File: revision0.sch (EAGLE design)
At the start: 93 parts, among them IC1 MSP430FR698X(1)80-PIN_PN, IC3 FT232RL

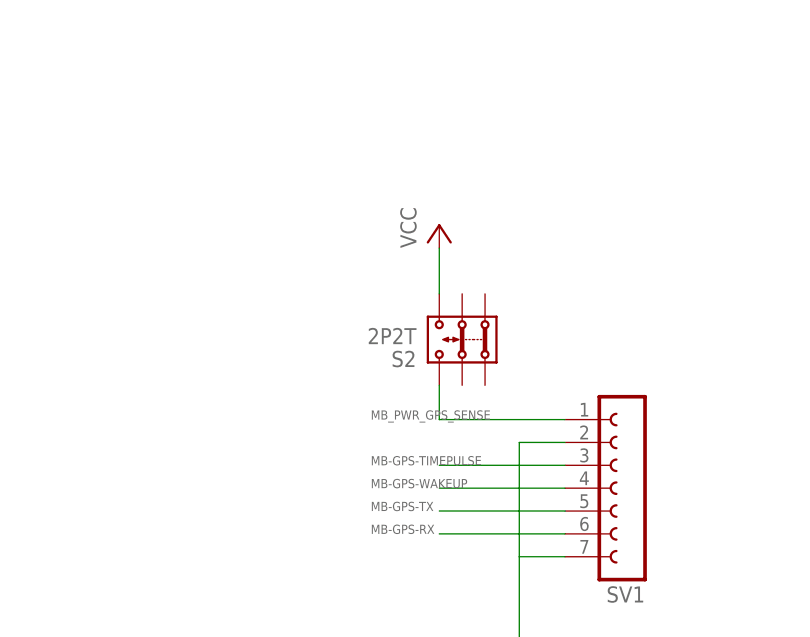
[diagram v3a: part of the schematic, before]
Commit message: Fix CANAL sliding switch
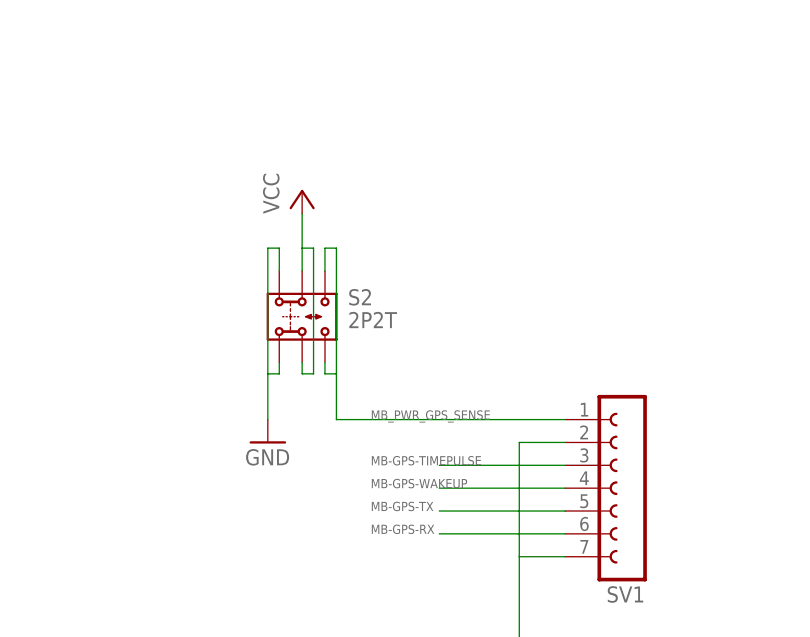
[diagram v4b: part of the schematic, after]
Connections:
- net GND: now also S2.1.1, S2.1.2
- net MB_PWR_GPS_SENSE: now also S2.3.2
- net VCC: now also S2.2.1, S2.2.2; no longer S2.3.2
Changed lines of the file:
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@@
 <grid distance="50" unitdist="mil" unit="mil" style="lines" multiple="1" display="yes" altdistance="0.01" altunitdist="inch" altunit="inch"/>
 <layers>
-<layer number="1" name="Top" color="4" fill="1" visible="no" active="no"/>
-<layer number="16" name="Bottom" color="1" fill="1" visible="no" active="no"/>
-<layer number="17" name="Pads" color="2" fill="1" visible="no" active="no"/>
-<layer number="18" name="Vias" color="2" fill="1" visible="no" active="no"/>
-<layer number="19" name="Unrouted" color="6" fill="1" visible="no" active="no"/>
-<layer number="20" name="Dimension" color="15" fill="1" visible="no" active="no"/>
-<layer number="21" name="tPlace" color="7" fill="1" visible="no" active="no"/>
-<layer number="22" name="bPlace" color="7" fill="1" visible="no" active="no"/>
-<layer number="23" name="tOrigins" color="15" fill="1" visible="no" active="no"/>
-<layer number="24" name="bOrigins" color="15" fill="1" visible="no" active="no"/>
-<layer number="25" name="tNames" color="7" fill="1" visible="no" active="no"/>
-<layer number="26" name="bNames" color="7" fill="1" visible="no" active="no"/>
-<layer number="27" name="tValues" color="7" fill="1" visible="no" active="no"/>
-<layer number="28" name="bValues" color="7" fill="1" visible="no" active="no"/>
+<layer number="1" name="Top" color="4" fill="1" visible="yes" active="no"/>
+<layer number="16" name="Bottom" color="1" fill="1" visible="yes" active="no"/>
+<layer number="17" name="Pads" color="2" fill="1" visible="yes" active="no"/>
+<layer number="18" name="Vias" color="2" fill="1" visible="yes" active="no"/>
+<layer number="19" name="Unrouted" color="6" fill="1" visible="yes" active="no"/>
+<layer number="20" name="Dimension" color="15" fill="1" visible="yes" active="no"/>
+<layer number="21" name="tPlace" color="7" fill="1" visible="yes" active="no"/>
+<layer number="22" name="bPlace" color="7" fill="1" visible="yes" active="no"/>
+<layer number="23" name="tOrigins" color="15" fill="1" visible="yes" active="no"/>
+<layer number="24" name="bOrigins" color="15" fill="1" visible="yes" active="no"/>
+<layer number="25" name="tNames" color="7" fill="1" visible="yes" active="no"/>
+<layer number="26" name="bNames" color="7" fill="1" visible="yes" active="no"/>
+<layer number="27" name="tValues" color="7" fill="1" visible="yes" active="no"/>
+<layer number="28" name="bValues" color="7" fill="1" visible="yes" active="no"/>
 <layer number="29" name="tStop" color="7" fill="3" visible="no" active="no"/>
 <layer number="30" name="bStop" color="7" fill="6" visible="no" active="no"/>
@@
 <layer number="35" name="tGlue" color="7" fill="4" visible="no" active="no"/>
 <layer number="36" name="bGlue" color="7" fill="5" visible="no" active="no"/>
-<layer number="37" name="tTest" color="7" fill="1" visible="no" active="no"/>
-<layer number="38" name="bTest" color="7" fill="1" visible="no" active="no"/>
+<layer number="37" name="tTest" color="7" fill="1" visible="yes" active="no"/>
+<layer number="38" name="bTest" color="7" fill="1" visible="yes" active="no"/>
 <layer number="39" name="tKeepout" color="4" fill="11" visible="no" active="no"/>
 <layer number="40" name="bKeepout" color="1" fill="11" visible="no" active="no"/>
@@
 <layer number="44" name="Drills" color="7" fill="1" visible="no" active="no"/>
 <layer number="45" name="Holes" color="7" fill="1" visible="no" active="no"/>
-<layer number="46" name="Milling" color="3" fill="1" visible="no" active="no"/>
-<layer number="47" name="Measures" color="7" fill="1" visible="no" active="no"/>
-<layer number="48" name="Document" color="7" fill="1" visible="no" active="no"/>
-<layer number="49" name="Reference" color="7" fill="1" visible="no" active="no"/>
-<layer number="51" name="tDocu" color="7" fill="1" visible="no" active="no"/>
-<layer number="52" name="bDocu" color="7" fill="1" visible="no" active="no"/>
+<layer number="46" name="Milling" color="3" fill="1" visible="yes" active="no"/>
+<layer number="47" name="Measures" color="7" fill="1" visible="yes" active="no"/>
+<layer number="48" name="Document" color="7" fill="1" visible="yes" active="no"/>
+<layer number="49" name="Reference" color="7" fill="1" visible="yes" active="no"/>
+<layer number="51" name="tDocu" color="7" fill="1" visible="yes" active="no"/>
+<layer number="52" name="bDocu" color="7" fill="1" visible="yes" active="no"/>
 <layer number="90" name="Modules" color="5" fill="1" visible="yes" active="yes"/>
 <layer number="91" name="Nets" color="2" fill="1" visible="yes" active="yes"/>
@@
 <part name="GND7" library="supply1" deviceset="GND" device=""/>
 <part name="GND12" library="supply1" deviceset="GND" device=""/>
+<part name="GND34" library="supply1" deviceset="GND" device=""/>
 </parts>
 <sheets>
@@
 <instance part="GND6" gate="1" x="-190.5" y="-17.78" rot="R270"/>
 <instance part="P+1" gate="VCC" x="-193.04" y="-35.56" rot="R90"/>
-<instance part="P+3" gate="VCC" x="180.34" y="73.66"/>
+<instance part="P+3" gate="VCC" x="165.1" y="77.47"/>
 <instance part="C3" gate="G$1" x="-175.26" y="-25.4" rot="MR0"/>
 <instance part="C4" gate="G$1" x="-182.88" y="-25.4" rot="MR0"/>
@@
 <instance part="TP-PWRBATT" gate="G$1" x="228.6" y="124.46"/>
 <instance part="GND26" gate="1" x="-119.38" y="-104.14"/>
-<instance part="S2" gate="G$1" x="182.88" y="60.96" rot="R180"/>
+<instance part="S2" gate="G$1" x="165.1" y="63.5"/>
 <instance part="R24" gate="G$1" x="220.98" y="-55.88" rot="R90"/>
 <instance part="R25" gate="G$1" x="213.36" y="-55.88" rot="R90"/>
@@
 <instance part="GND7" gate="1" x="250.19" y="24.13"/>
 <instance part="GND12" gate="1" x="281.94" y="-88.9"/>
+<instance part="GND34" gate="1" x="161.29" y="49.53"/>
 </instances>
 <busses>
@@
 <wire x1="276.86" y1="219.71" x2="276.86" y2="224.79" width="0.1524" layer="91"/>
 <pinref part="JP2" gate="A" pin="2"/>
-</segment>
-<segment>
-<pinref part="P+3" gate="VCC" pin="VCC"/>
-<pinref part="S2" gate="G$1" pin="3.2"/>
-<wire x1="180.34" y1="66.04" x2="180.34" y2="71.12" width="0.1524" layer="91"/>
 </segment>
 <segment>
@@
 <junction x="-449.58" y="38.1"/>
 </segment>
+<segment>
+<pinref part="P+3" gate="VCC" pin="VCC"/>
+<wire x1="165.1" y1="74.93" x2="165.1" y2="71.12" width="0.1524" layer="91"/>
+<pinref part="S2" gate="G$1" pin="2.1"/>
+<wire x1="165.1" y1="71.12" x2="165.1" y2="68.58" width="0.1524" layer="91"/>
+<wire x1="165.1" y1="71.12" x2="166.37" y2="71.12" width="0.1524" layer="91"/>
+<wire x1="166.37" y1="71.12" x2="166.37" y2="57.15" width="0.1524" layer="91"/>
+<pinref part="S2" gate="G$1" pin="2.2"/>
+<wire x1="166.37" y1="57.15" x2="165.1" y2="57.15" width="0.1524" layer="91"/>
+<wire x1="165.1" y1="57.15" x2="165.1" y2="58.42" width="0.1524" layer="91"/>
+</segment>
 </net>
 <net name="GND" class="0">
@@
 <wire x1="250.19" y1="39.37" x2="250.19" y2="26.67" width="0.1524" layer="91"/>
 <wire x1="257.81" y1="39.37" x2="250.19" y2="39.37" width="0.1524" layer="91"/>
+</segment>
+<segment>
+<pinref part="S2" gate="G$1" pin="1.1"/>
+<wire x1="162.56" y1="68.58" x2="162.56" y2="71.12" width="0.1524" layer="91"/>
+<wire x1="162.56" y1="71.12" x2="161.29" y2="71.12" width="0.1524" layer="91"/>
+<wire x1="161.29" y1="71.12" x2="161.29" y2="57.15" width="0.1524" layer="91"/>
+<pinref part="S2" gate="G$1" pin="1.2"/>
+<wire x1="161.29" y1="57.15" x2="162.56" y2="57.15" width="0.1524" layer="91"/>
+<wire x1="162.56" y1="57.15" x2="162.56" y2="58.42" width="0.1524" layer="91"/>
+<pinref part="GND34" gate="1" pin="GND"/>
+<wire x1="161.29" y1="52.07" x2="161.29" y2="57.15" width="0.1524" layer="91"/>
 </segment>
 </net>
@@
 </segment>
 <segment>
-<wire x1="180.34" y1="52.07" x2="194.31" y2="52.07" width="0.1524" layer="91"/>
 <label x="172.72" y="52.07" size="1.016" layer="95"/>
+<pinref part="S2" gate="G$1" pin="3.2"/>
+<wire x1="167.64" y1="58.42" x2="167.64" y2="57.15" width="0.1524" layer="91"/>
 <pinref part="S2" gate="G$1" pin="3.1"/>
-<wire x1="180.34" y1="52.07" x2="180.34" y2="55.88" width="0.1524" layer="91"/>
+<wire x1="167.64" y1="68.58" x2="167.64" y2="71.12" width="0.1524" layer="91"/>
+<wire x1="167.64" y1="71.12" x2="168.91" y2="71.12" width="0.1524" layer="91"/>
+<wire x1="168.91" y1="71.12" x2="168.91" y2="57.15" width="0.1524" layer="91"/>
+<wire x1="168.91" y1="57.15" x2="167.64" y2="57.15" width="0.1524" layer="91"/>
 <pinref part="SV1" gate="G$1" pin="1"/>
-</segment>
-</net>
+<wire x1="168.91" y1="52.07" x2="194.31" y2="52.07" width="0.1524" layer="91"/>
+<wire x1="168.91" y1="52.07" x2="168.91" y2="57.15" width="0.1524" layer="91"/>
+</segment>
+</net>

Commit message: Add MWSL1251 antenna to taGPS design
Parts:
- removed R18, R19, R20, R21: 470k, tagps:R-EU_R0805
- removed TP-VCCSTAT: TPSQPAD1-13, tagps:TPSQPAD1-13
- added C13: 100n, tagps:C-EUC0805
- added C14: 1u, tagps:C-EUC0805
- added FB4, FB5, FB6, R34, R35: 0, tagps:R-EU_R0805
- added R17, R33: 100k, tagps:R-EU_R0805
- added TP-GPSPWR1, TP-GPSRX1, TP-GPSTX1: TPSQTP10R, tagps:TPSQTP10R
- added U$5: MWSL1251, tagps:MWSL1251
- added U$6: MAX-8C-0, tagps:MAX-8C-0
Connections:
- removed net MB_PWR_GPS_SENSE: IC1.P2.2/UCA0CLK/TB0.4/RTCCLK/S16, S2.3.1, S2.3.2, SV1.1
- removed net N$28: R20.2, U$2.WARN2
- removed net N$29: R19.2, U$2.WARN1
- removed net N$30: R18.2, U$2.STAT1
- removed net N$31: R18.1, R19.1, R20.1, R21.1, TP-VCCSTAT.TP
- new net MB-PWR_GPS_SENSE: C13.2, C14.1, IC1.P2.2/UCA0CLK/TB0.4/RTCCLK/S16, R17.2, R33.2, S2.3.1, S2.3.2, SV1.1, TP-GPSPWR1.TP, U$6.VCC, U$6.VCC_IO, U$6.V_BCKP
- new net N$46: R34.2, U$6.EXTINT
- new net N$47: FB6.2, R35.2
- new net N$48: FB4.1, U$6.RXD
- new net N$49: FB5.1, U$6.TXD
- new net N$50: FB6.1, U$6.TIMEPULSE
- net GND: now also C13.1, C14.2, U$5.GND, U$6.GND
- net MB-GPS-RX: now also FB4.2, R17.1, TP-GPSRX1.TP
- net MB-GPS-TIMEPULSE: now also R35.1
- net MB-GPS-TX: now also FB5.2, R33.1, TP-GPSTX1.TP
- net MB-GPS-WAKEUP: now also R34.1
- net N$27: now also U$5.FEED, U$6.RF_IN; no longer R21.2, U$2.STAT2

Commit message: Add ceramic antenna, move the patch antenna connetor a bit
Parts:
- added C23: 100n, tagps:C-EUC0805
- added C29: 1u, tagps:C-EUC0805
- added U$7: MAX-8C-0, tagps:MAX-8C-0
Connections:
- removed net N$48: FB4.1, U$6.RXD
- new net N$15: FB4.1, U$6.RXD, U$7.RXD
- net GND: now also C23.1, C29.2, U$7.GND
- net MB-PWR_GPS_SENSE: now also C23.2, C29.1, U$7.VCC, U$7.VCC_IO, U$7.V_BCKP
- net N$46: now also U$7.EXTINT
- net N$49: now also U$7.TXD
- net N$50: now also U$7.TIMEPULSE
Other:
- moved on the sheet: C13, C14, FB4, FB5, FB6, R17, R33, R34, R35, TP-GPSPWR1, TP-GPSRX1, TP-GPSTX1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

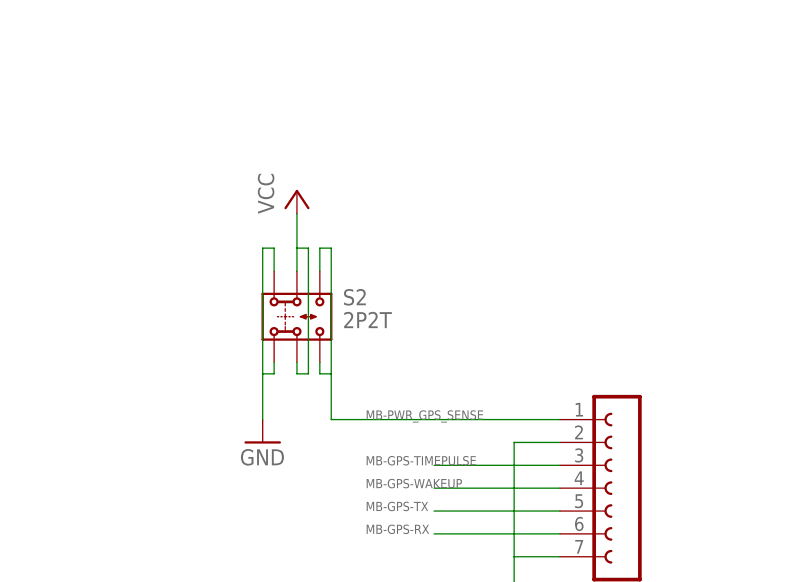
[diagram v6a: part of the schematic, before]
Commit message: Fix gps-power switch scheme
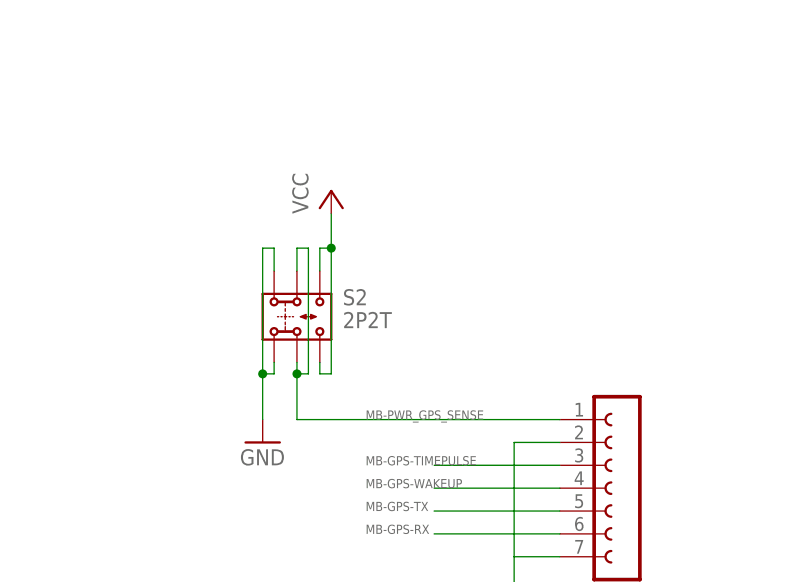
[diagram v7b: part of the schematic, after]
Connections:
- net MB-PWR_GPS_SENSE: now also S2.2.1, S2.2.2; no longer S2.3.1, S2.3.2
- net VCC: now also S2.3.1, S2.3.2; no longer S2.2.1, S2.2.2
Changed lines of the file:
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@@
 <instance part="GND6" gate="1" x="-190.5" y="-17.78" rot="R270"/>
 <instance part="P+1" gate="VCC" x="-193.04" y="-35.56" rot="R90"/>
-<instance part="P+3" gate="VCC" x="165.1" y="77.47"/>
+<instance part="P+3" gate="VCC" x="168.91" y="77.47"/>
 <instance part="C3" gate="G$1" x="-175.26" y="-25.4" rot="MR0"/>
 <instance part="C4" gate="G$1" x="-182.88" y="-25.4" rot="MR0"/>
@@
 </segment>
 <segment>
+<pinref part="S2" gate="G$1" pin="3.2"/>
+<wire x1="167.64" y1="58.42" x2="167.64" y2="57.15" width="0.1524" layer="91"/>
+<pinref part="S2" gate="G$1" pin="3.1"/>
+<wire x1="167.64" y1="68.58" x2="167.64" y2="71.12" width="0.1524" layer="91"/>
+<wire x1="167.64" y1="71.12" x2="168.91" y2="71.12" width="0.1524" layer="91"/>
+<wire x1="168.91" y1="71.12" x2="168.91" y2="57.15" width="0.1524" layer="91"/>
+<wire x1="168.91" y1="57.15" x2="167.64" y2="57.15" width="0.1524" layer="91"/>
 <pinref part="P+3" gate="VCC" pin="VCC"/>
-<wire x1="165.1" y1="74.93" x2="165.1" y2="71.12" width="0.1524" layer="91"/>
-<pinref part="S2" gate="G$1" pin="2.1"/>
-<wire x1="165.1" y1="71.12" x2="165.1" y2="68.58" width="0.1524" layer="91"/>
-<wire x1="165.1" y1="71.12" x2="166.37" y2="71.12" width="0.1524" layer="91"/>
-<wire x1="166.37" y1="71.12" x2="166.37" y2="57.15" width="0.1524" layer="91"/>
-<pinref part="S2" gate="G$1" pin="2.2"/>
-<wire x1="166.37" y1="57.15" x2="165.1" y2="57.15" width="0.1524" layer="91"/>
-<wire x1="165.1" y1="57.15" x2="165.1" y2="58.42" width="0.1524" layer="91"/>
+<wire x1="168.91" y1="74.93" x2="168.91" y2="71.12" width="0.1524" layer="91"/>
+<junction x="168.91" y="71.12"/>
 </segment>
 </net>
@@
 <pinref part="GND34" gate="1" pin="GND"/>
 <wire x1="161.29" y1="52.07" x2="161.29" y2="57.15" width="0.1524" layer="91"/>
+<junction x="161.29" y="57.15"/>
 </segment>
 <segment>
@@
 <segment>
 <label x="172.72" y="52.07" size="1.016" layer="95"/>
-<pinref part="S2" gate="G$1" pin="3.2"/>
-<wire x1="167.64" y1="58.42" x2="167.64" y2="57.15" width="0.1524" layer="91"/>
-<pinref part="S2" gate="G$1" pin="3.1"/>
-<wire x1="167.64" y1="68.58" x2="167.64" y2="71.12" width="0.1524" layer="91"/>
-<wire x1="167.64" y1="71.12" x2="168.91" y2="71.12" width="0.1524" layer="91"/>
-<wire x1="168.91" y1="71.12" x2="168.91" y2="57.15" width="0.1524" layer="91"/>
-<wire x1="168.91" y1="57.15" x2="167.64" y2="57.15" width="0.1524" layer="91"/>
 <pinref part="SV1" gate="G$1" pin="1"/>
-<wire x1="168.91" y1="52.07" x2="194.31" y2="52.07" width="0.1524" layer="91"/>
-<wire x1="168.91" y1="52.07" x2="168.91" y2="57.15" width="0.1524" layer="91"/>
-</segment>
-<segment>
+<wire x1="165.1" y1="52.07" x2="194.31" y2="52.07" width="0.1524" layer="91"/>
+<pinref part="S2" gate="G$1" pin="2.1"/>
+<wire x1="165.1" y1="71.12" x2="165.1" y2="68.58" width="0.1524" layer="91"/>
+<wire x1="165.1" y1="71.12" x2="166.37" y2="71.12" width="0.1524" layer="91"/>
+<wire x1="166.37" y1="71.12" x2="166.37" y2="57.15" width="0.1524" layer="91"/>
+<pinref part="S2" gate="G$1" pin="2.2"/>
+<wire x1="166.37" y1="57.15" x2="165.1" y2="57.15" width="0.1524" layer="91"/>
+<wire x1="165.1" y1="57.15" x2="165.1" y2="58.42" width="0.1524" layer="91"/>
+<wire x1="165.1" y1="52.07" x2="165.1" y2="57.15" width="0.1524" layer="91"/>
+<junction x="165.1" y="57.15"/>
+</segment>
+<segment>
